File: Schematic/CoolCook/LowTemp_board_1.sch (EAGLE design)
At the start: 31 parts, among them IC1 7805L, J1 SCREEN, SW2 EC11B-V

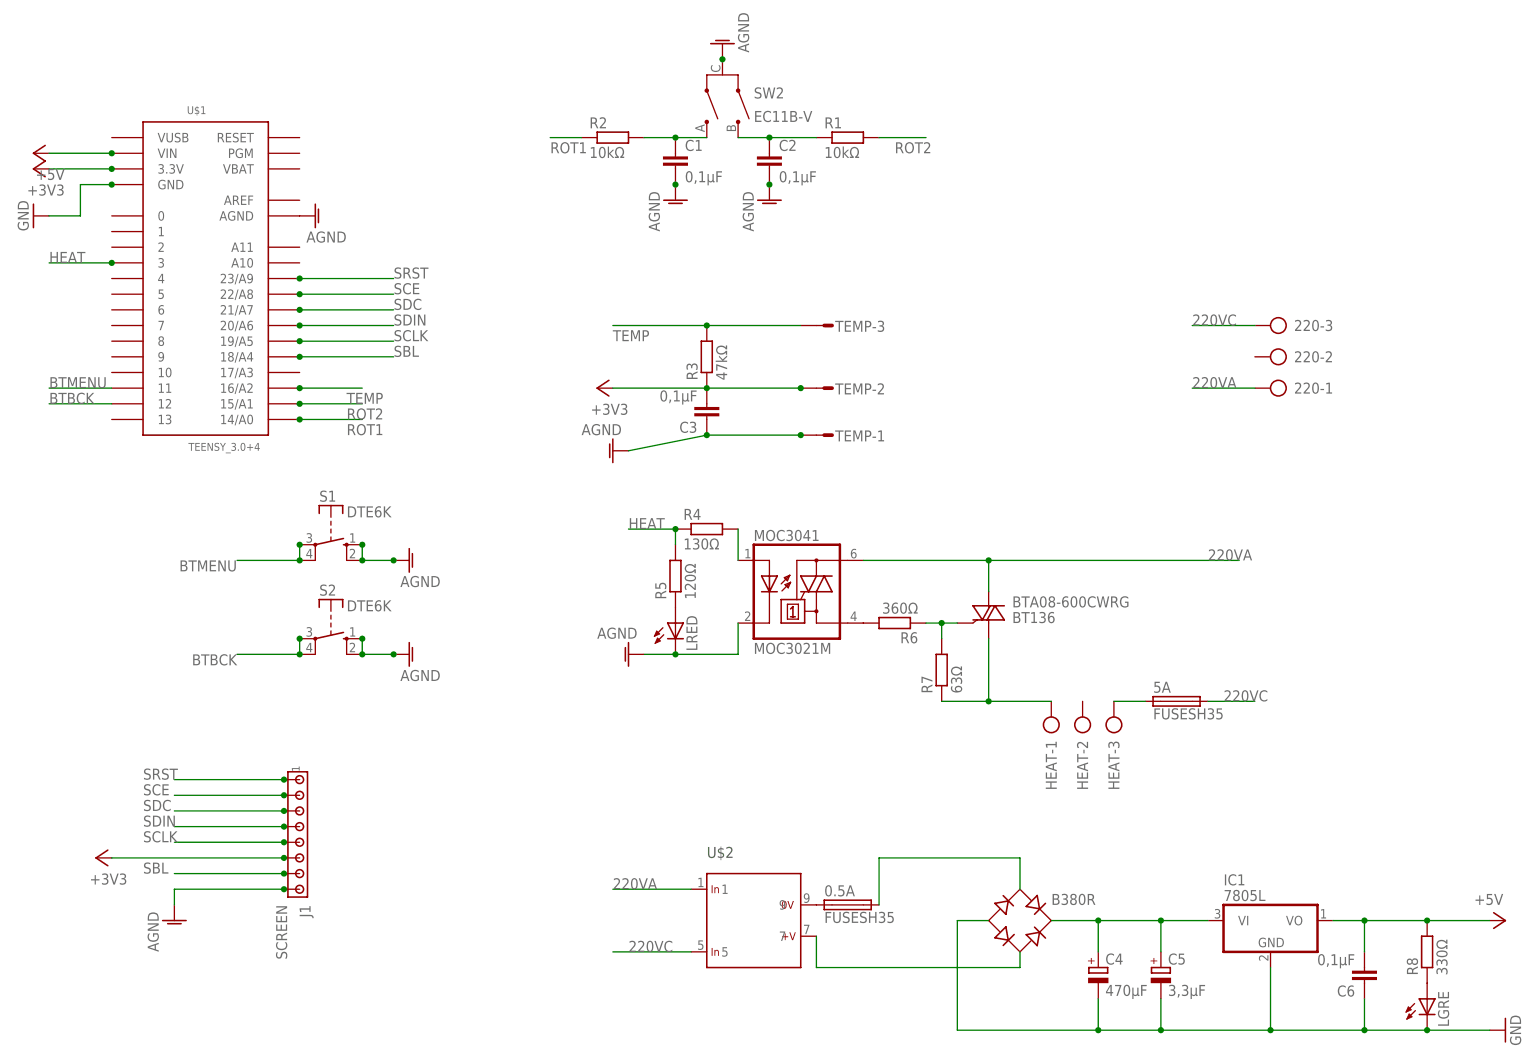
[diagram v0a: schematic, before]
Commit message: Add 2 board schematic. One board for the controls (screen / button) One board for electronics part
Each board areBoards are connected together with 2x10 pin connector
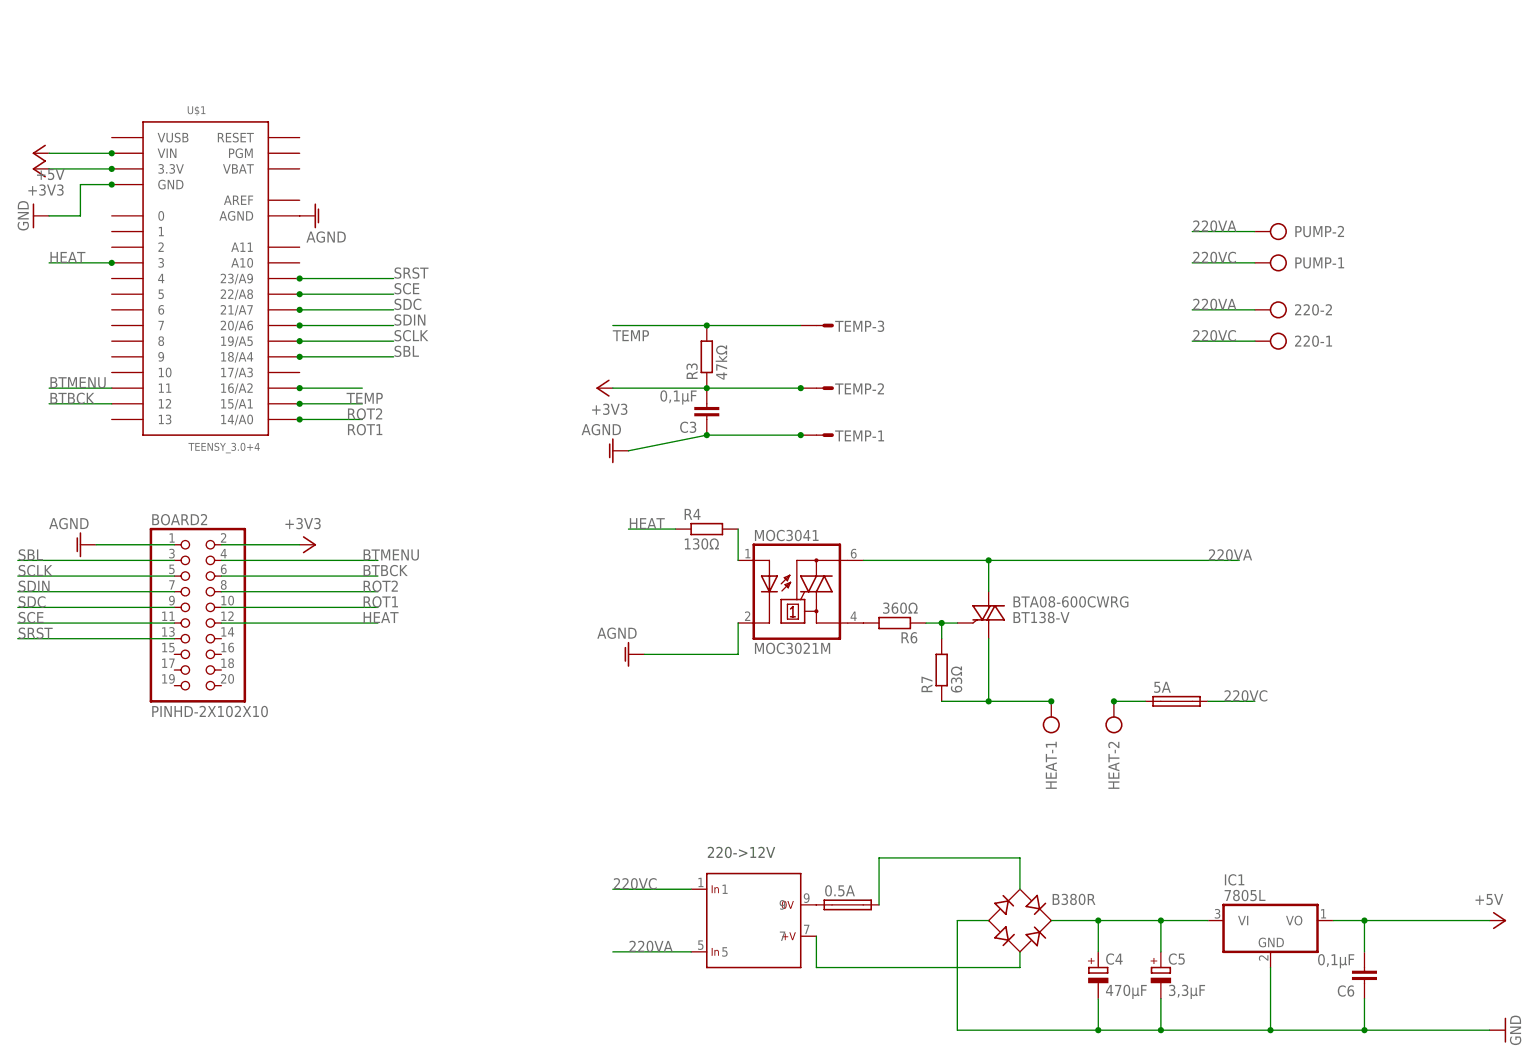
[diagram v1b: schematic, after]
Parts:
- removed C1, C2: 0,1µF, resistor:C-EU050-025X075
- removed J1: SCREEN, con-amp:MTA08-100
- removed LGRE, LRED: (no value), led:LED5MM
- removed R1, R2: 10kΩ, resistor:R-EU_0207/10
- removed R5: 120Ω, resistor:R-EU_0207/10
- removed R8: 330Ω, resistor:R-EU_0207/10
- removed S1, S2: DTE6K, switch-misc:DTE6K
- removed SW2: EC11B-V, alps:EC11B-V
- added BOARD2: PINHD-2X102X10, adafruit:PINHD-2X102X10
- added PUMP: (no value), con-ptr500:AK500/2-H
- 0.5A, 5A: value FUSESH35 -> (none); device fuse:FUSESH35 -> fuse:SH22,5A
- 220, HEAT: device con-ptr500:AK500/3-H -> con-ptr500:AK500/2-H
- BTA08-600CWRG: value BT136 -> BT138-V; device triac:BT136 -> triac:BT138-V
- R3, R4, R6, R7: device resistor:R-EU_0207/10 -> resistor:R-EU_0207/7
- TEMP: device con-amp-mt:L03P -> con-amp-mt:S03P
- renumbered U$2 to 220->12V
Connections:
- removed net N$1: C1.1, R2.2, SW2.A
- removed net N$15: LGRE.A, R8.1
- removed net N$2: C2.1, R1.1, SW2.B
- removed net N$4: LRED.A, R5.1
- net +3V3: now also BOARD2.2; no longer J1.6
- net +5V: no longer R8.2
- net 220VA: now also 220-2.KL, 220->12V.5, PUMP-2.KL; no longer 220-1.KL, 220->12V.1
- net 220VC: now also 220-1.KL, 220->12V.1, PUMP-1.KL; no longer 220-3.KL, 220->12V.5
- net AGND: now also BOARD2.1; no longer C1.2, C2.2, J1.8, LRED.C, S1.S, S1.S@1, S2.S, S2.S@1, SW2.C
- net BTBCK: now also BOARD2.6; no longer S2.P, S2.P@1
- net BTMENU: now also BOARD2.4; no longer S1.P, S1.P@1
- net GND: no longer LGRE.C
- net HEAT: now also BOARD2.12; no longer R5.2
- net N$9: now also HEAT-2.KL; no longer HEAT-3.KL
- net ROT1: now also BOARD2.10; no longer R2.1
- net ROT2: now also BOARD2.8; no longer R1.2
- net SBL: now also BOARD2.3; no longer J1.7
- net SCE: now also BOARD2.11; no longer J1.2
- net SCLK: now also BOARD2.5; no longer J1.5
- net SDC: now also BOARD2.9; no longer J1.3
- net SDIN: now also BOARD2.7; no longer J1.4
- net SRST: now also BOARD2.13; no longer J1.1
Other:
- moved on the sheet: 220-1, 220-2, HEAT-2
